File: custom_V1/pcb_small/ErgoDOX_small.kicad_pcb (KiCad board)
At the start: 2 copper layers, 74.3 x 50 mm, 61 parts, among them J1 Input, J10 Conn_01x01, J11 Conn_01x01, J12 Conn_01x01, J13 Conn_01x01, J14 Conn_01x01, J15 Conn_01x01, J16 Conn_01x01, J17 Conn_01x01, J18 Conn_01x01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

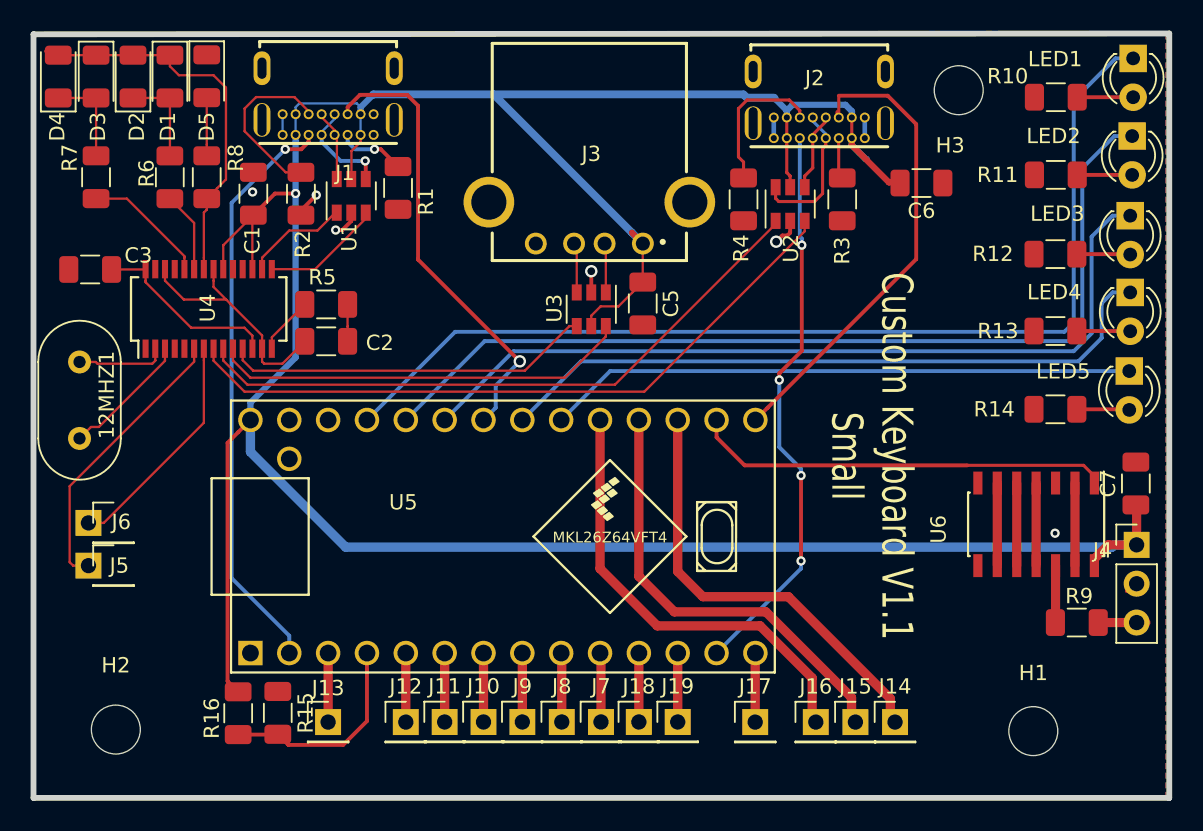
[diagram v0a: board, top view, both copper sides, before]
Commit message: add 1 mcu
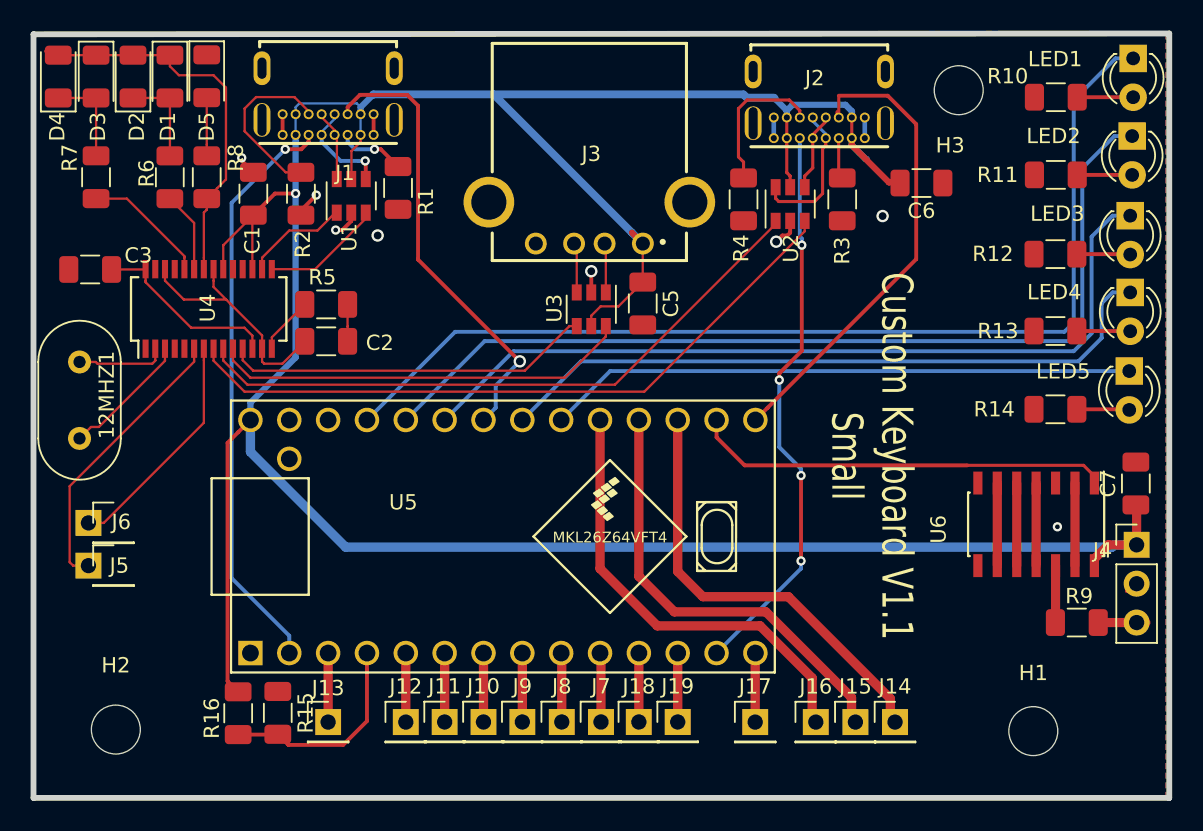
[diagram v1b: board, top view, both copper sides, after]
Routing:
- net GND: track 13.4 -> 17.6 mm, vias 6 -> 8
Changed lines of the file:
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@@
     (thickness 1.6002)
     (drawings 10)
-    (tracks 410)
+    (tracks 417)
     (zones 0)
     (modules 61)
@@
   (segment (start 102.1715 70.485) (end 102.1715 74.9935) (width 0.6096) (layer Front) (net 10))
   (segment (start 99.6315 70.485) (end 99.6315 74.9935) (width 0.6096) (layer Front) (net 11))
-  (via (at 126.8476 62.6491) (size 0.6096) (drill 0.3048) (layers Front Back) (net 12))
+  (via (at 127 62.23) (size 0.6096) (drill 0.3048) (layers Front Back) (net 12))
   (segment (start 131.579114 66.386455) (end 131.515614 66.449955) (width 0.2032) (layer Front) (net 12))
   (segment (start 114.4048 36.8164) (end 114.4048 35.4664) (width 0.3048) (layer Back) (net 12))
@@
   (segment (start 77.5335 41.5417) (end 78.5368 40.5384) (width 0.254) (layer Front) (net 12))
   (segment (start 77.5335 41.849499) (end 77.5335 41.5417) (width 0.254) (layer Front) (net 12))
-  (via (at 74.3712 40.3352) (size 0.6096) (drill 0.3048) (layers Front Back) (net 12))
+  (via (at 73.66 38.1) (size 0.6096) (drill 0.3048) (layers Front Back) (net 12))
+  (via (at 115.57 41.91) (size 0.8128) (drill 0.508) (layers Front Back) (net 12))
+  (segment (start 82.2865 36.6005) (end 82.2865 35.2505) (width 0.254) (layer Front) (net 12))
+  (segment (start 73.66 38.2875) (end 74.422 39.0495) (width 0.254) (layer Front) (net 12))
+  (segment (start 73.66 38.1) (end 73.66 38.2875) (width 0.254) (layer Front) (net 12))
+  (via (at 82.55 43.18) (size 0.8128) (drill 0.508) (layers Front Back) (net 12))
+  (segment (start 76.3365 36.7114) (end 76.429699 36.804599) (width 0.254) (layer Front) (net 12))
+  (segment (start 76.3365 35.2505) (end 76.3365 36.7114) (width 0.254) (layer Front) (net 12))
   (segment (start 109.3048 36.8164) (end 109.3048 35.4664) (width 0.2032) (layer Front) (net 13))
   (segment (start 113.5548 36.8164) (end 113.5548 35.4664) (width 0.2032) (layer Front) (net 13))
@@
   (segment (start 112.6998 36.8214) (end 112.7048 36.8164) (width 0.2032) (layer Front) (net 27))
   (segment (start 112.6998 38.8844) (end 112.6998 36.8214) (width 0.2032) (layer Front) (net 27))
-  (segment (start 97.388 43.709) (end 97.393 43.709) (width 0.1524) (layer Back) (net 29))
-  (segment (start 97.393 43.958) (end 97.393 43.709) (width 0.1524) (layer Back) (net 29))
   (segment (start 95.5675 46.9035) (end 95.57 46.906) (width 0.1524) (layer Front) (net 28))
   (segment (start 95.57 43.886) (end 95.393 43.709) (width 0.1524) (layer Front) (net 28))
   (segment (start 95.57 46.906) (end 95.57 43.886) (width 0.1524) (layer Front) (net 28))
+  (segment (start 97.388 43.709) (end 97.393 43.709) (width 0.1524) (layer Back) (net 29))
+  (segment (start 97.393 43.958) (end 97.393 43.709) (width 0.1524) (layer Back) (net 29))
   (segment (start 97.47 43.786) (end 97.393 43.709) (width 0.1524) (layer Front) (net 29))
   (segment (start 97.47 46.906) (end 97.47 43.786) (width 0.1524) (layer Front) (net 29))
@@
   (segment (start 130.6085 46.902737) (end 131.7625 46.902737) (width 0.254) (layer Back) (net 31))
   (segment (start 92.0115 55.245) (end 95.8469 51.4096) (width 0.254) (layer Back) (net 31))
-  (segment (start 89.4715 70.485) (end 89.4715 74.9935) (width 0.6096) (layer Front) (net 35))
-  (segment (start 92.0115 74.9935) (end 92.0115 70.485) (width 0.6096) (layer Front) (net 36))
-  (segment (start 131.6355 52.109737) (end 131.699 52.046237) (width 0.2032) (layer Front) (net 39))
   (segment (start 131.699 41.822737) (end 131.7625 41.886237) (width 0.2032) (layer Front) (net 32))
   (segment (start 86.9315 55.245) (end 91.4273 50.7492) (width 0.254) (layer Back) (net 32))
@@
   (segment (start 87.6173 49.4792) (end 127.4572 49.4792) (width 0.254) (layer Back) (net 34))
   (segment (start 81.8515 55.245) (end 87.6173 49.4792) (width 0.254) (layer Back) (net 34))
+  (segment (start 89.4715 70.485) (end 89.4715 74.9935) (width 0.6096) (layer Front) (net 35))
+  (segment (start 92.0115 74.9935) (end 92.0115 70.485) (width 0.6096) (layer Front) (net 36))
+  (segment (start 131.6355 52.109737) (end 131.699 52.046237) (width 0.2032) (layer Front) (net 39))
   (segment (start 97.750263 52.046237) (end 131.699 52.046237) (width 0.254) (layer Back) (net 39))
   (segment (start 94.5515 55.245) (end 97.750263 52.046237) (width 0.254) (layer Back) (net 39))
@@
   (segment (start 92.176524 52.022076) (end 95.0926 49.106) (width 0.1524) (layer Front) (net 49))
   (segment (start 74.410485 52.022076) (end 92.176524 52.022076) (width 0.1524) (layer Front) (net 49))
-  (segment (start 70.549675 50.583866) (end 70.549675 50.183432) (width 0.1524) (layer Front) (net 59))
-  (segment (start 70.549675 50.183432) (end 70.495676 50.129433) (width 0.1524) (layer Front) (net 59))
+  (segment (start 73.078937 50.573128) (end 73.089675 50.583866) (width 0.2032) (layer Front) (net 50))
+  (segment (start 94.779114 52.479286) (end 97.47 49.7884) (width 0.1524) (layer Front) (net 50))
+  (segment (start 97.47 49.7884) (end 97.47 49.106) (width 0.1524) (layer Front) (net 50))
+  (segment (start 74.221103 52.479286) (end 94.779114 52.479286) (width 0.1524) (layer Front) (net 50))
+  (segment (start 73.089675 51.347858) (end 74.221103 52.479286) (width 0.1524) (layer Front) (net 50))
+  (segment (start 73.089675 50.583866) (end 73.089675 51.347858) (width 0.1524) (layer Front) (net 50))
+  (segment (start 110.4748 42.905) (end 110.4748 42.2226) (width 0.1524) (layer Front) (net 51))
+  (segment (start 99.986094 53.393706) (end 110.4748 42.905) (width 0.1524) (layer Front) (net 51))
+  (segment (start 73.842339 53.393706) (end 99.986094 53.393706) (width 0.1524) (layer Front) (net 51))
+  (segment (start 71.819675 51.371042) (end 73.842339 53.393706) (width 0.1524) (layer Front) (net 51))
+  (segment (start 71.819675 50.583866) (end 71.819675 51.371042) (width 0.1524) (layer Front) (net 51))
+  (segment (start 108.5748 42.4276) (end 108.5748 42.2226) (width 0.1524) (layer Front) (net 52))
+  (segment (start 98.065904 52.936496) (end 108.5748 42.4276) (width 0.1524) (layer Front) (net 52))
+  (segment (start 72.454675 51.35945) (end 74.031721 52.936496) (width 0.1524) (layer Front) (net 52))
+  (segment (start 74.031721 52.936496) (end 98.065904 52.936496) (width 0.1524) (layer Front) (net 52))
+  (segment (start 72.454675 50.583866) (end 72.454675 51.35945) (width 0.1524) (layer Front) (net 52))
   (segment (start 79.8855 41.5845) (end 79.8855 41.3795) (width 0.1524) (layer Front) (net 53))
   (segment (start 78.614491 42.855509) (end 79.8855 41.5845) (width 0.1524) (layer Front) (net 53))
@@
   (segment (start 63.805499 55.701501) (end 64.325091 55.701501) (width 0.1524) (layer Front) (net 56))
   (segment (start 63.0555 56.4515) (end 63.805499 55.701501) (width 0.1524) (layer Front) (net 56))
-  (segment (start 73.078937 50.573128) (end 73.089675 50.583866) (width 0.2032) (layer Front) (net 50))
-  (segment (start 94.779114 52.479286) (end 97.47 49.7884) (width 0.1524) (layer Front) (net 50))
-  (segment (start 97.47 49.7884) (end 97.47 49.106) (width 0.1524) (layer Front) (net 50))
-  (segment (start 74.221103 52.479286) (end 94.779114 52.479286) (width 0.1524) (layer Front) (net 50))
-  (segment (start 73.089675 51.347858) (end 74.221103 52.479286) (width 0.1524) (layer Front) (net 50))
-  (segment (start 73.089675 50.583866) (end 73.089675 51.347858) (width 0.1524) (layer Front) (net 50))
-  (segment (start 110.4748 42.905) (end 110.4748 42.2226) (width 0.1524) (layer Front) (net 51))
-  (segment (start 99.986094 53.393706) (end 110.4748 42.905) (width 0.1524) (layer Front) (net 51))
-  (segment (start 73.842339 53.393706) (end 99.986094 53.393706) (width 0.1524) (layer Front) (net 51))
-  (segment (start 71.819675 51.371042) (end 73.842339 53.393706) (width 0.1524) (layer Front) (net 51))
-  (segment (start 71.819675 50.583866) (end 71.819675 51.371042) (width 0.1524) (layer Front) (net 51))
-  (segment (start 108.5748 42.4276) (end 108.5748 42.2226) (width 0.1524) (layer Front) (net 52))
-  (segment (start 98.065904 52.936496) (end 108.5748 42.4276) (width 0.1524) (layer Front) (net 52))
-  (segment (start 72.454675 51.35945) (end 74.031721 52.936496) (width 0.1524) (layer Front) (net 52))
-  (segment (start 74.031721 52.936496) (end 98.065904 52.936496) (width 0.1524) (layer Front) (net 52))
-  (segment (start 72.454675 50.583866) (end 72.454675 51.35945) (width 0.1524) (layer Front) (net 52))
+  (segment (start 70.549675 50.583866) (end 70.549675 50.183432) (width 0.1524) (layer Front) (net 59))
+  (segment (start 70.549675 50.183432) (end 70.495676 50.129433) (width 0.1524) (layer Front) (net 59))
   (segment (start 70.549675 51.336266) (end 70.549675 50.583866) (width 0.1524) (layer Front) (net 59))
   (segment (start 70.549675 51.434668) (end 70.549675 51.336266) (width 0.1524) (layer Front) (net 59))
